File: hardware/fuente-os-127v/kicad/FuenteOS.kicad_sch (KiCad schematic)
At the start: 10 parts, among them J1 127 VCA, J2 SALIDA OS

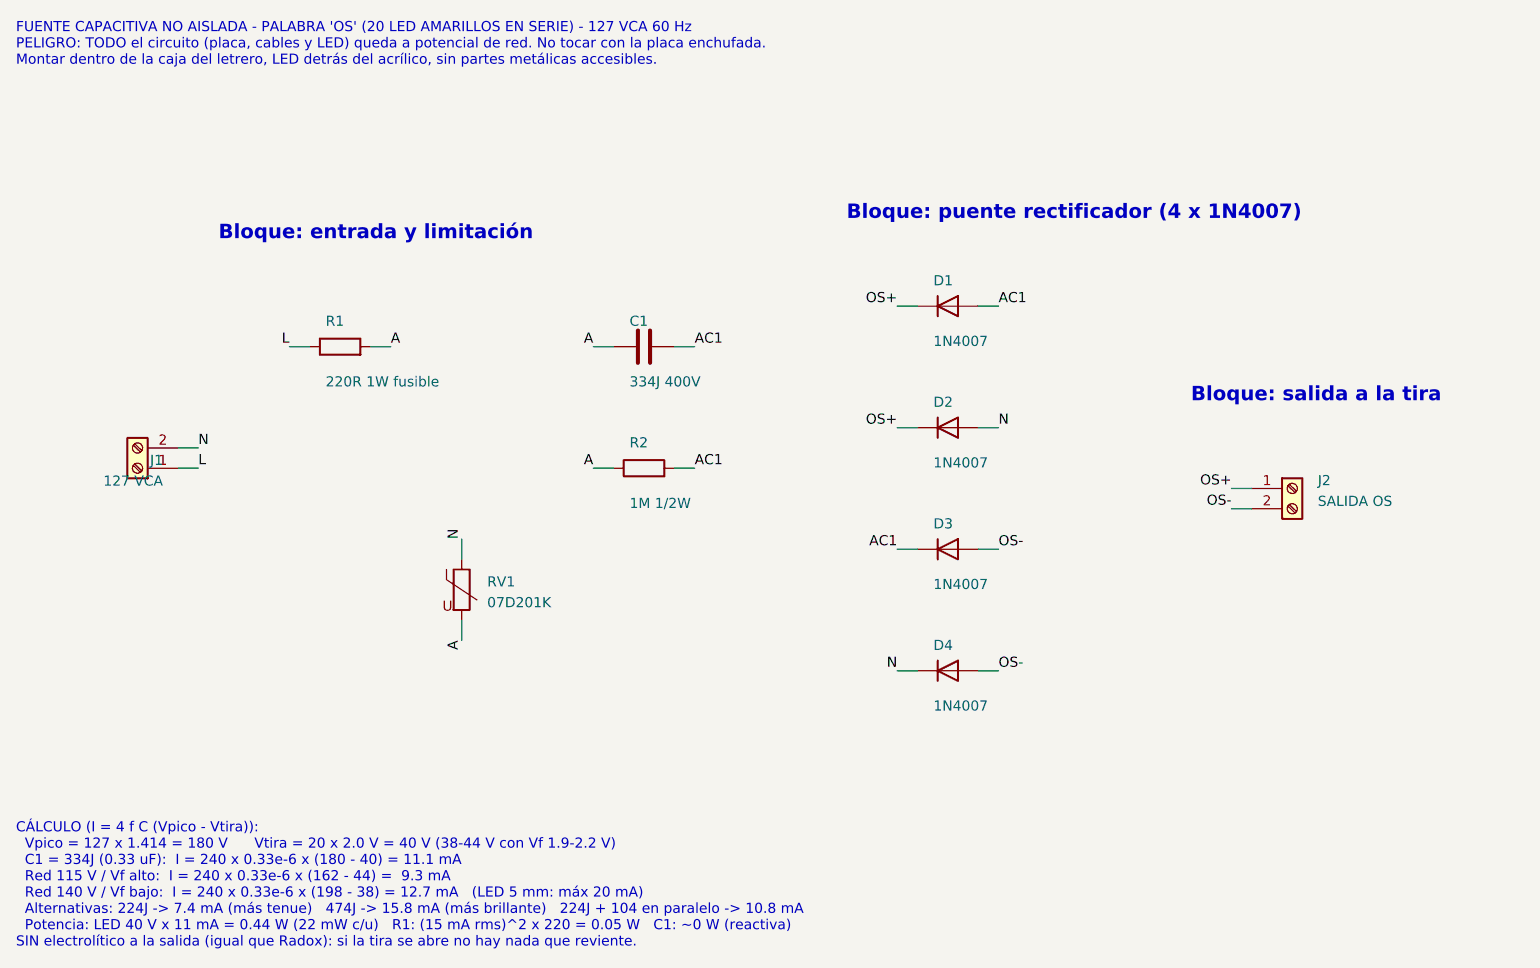
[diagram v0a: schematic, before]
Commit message: Placa OS v2 (27 LED, puente 2W10, capacitor paso 10/15 mm) y secuenciador de flechas 127 VCA
- fuente-os-127v: O (13) + S (14) = 27 LED; C1 334J -> 10 mA (474J si son blanco
  calido); puente redondo 2W10; huella de capacitor con barrenos a 10 y 15 mm.
- flechas-127v: NE555 + CD4017 + 3 SCR MCR100-6, dos fuentes capacitivas con
  2W10 (logica 474J + zener 12 V, flechas 224J ~8 mA). PCB 50x60 mm una cara,
  2 puentes de alambre; ERC/DRC 0 con paridad; PDF 1:1 para planchar, Gerber,
  Excellon, BOM.
- gen/comun.py: huellas, esquema, PCB, ruteo y separacion de redes por puentes
  compartidos por ambas placas.

Co-Authored-By: Claude Opus 5.5 <noreply@anthropic.com>
Claude-Session: https://claude.ai/code/session_01WVk3oGwfQfGTmAT2PMp8oW
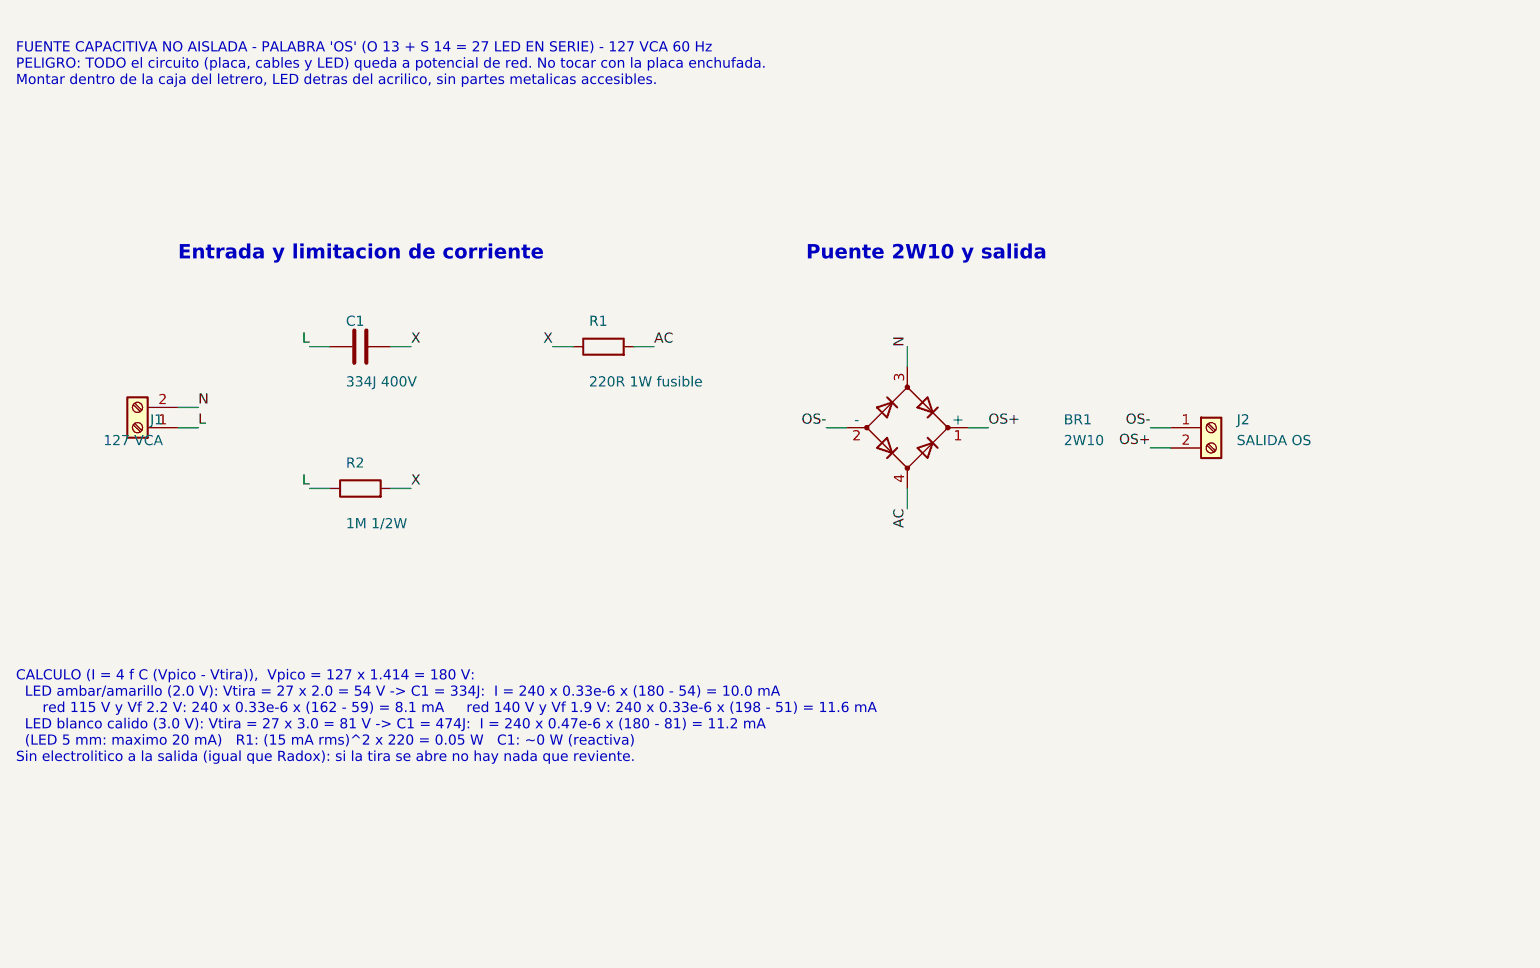
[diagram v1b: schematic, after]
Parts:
- removed D1, D2, D3, D4: 1N4007, FuenteOS:D_DO-41_P10.16mm, symbol Device:D
- removed RV1: 07D201K, FuenteOS:Varistor_D7mm_P5mm, symbol Device:Varistor
- added BR1: 2W10, FuenteOS:Puente_2W10, symbol Device:D_Bridge_+-AA
- C1: footprint FuenteOS:C_Poliester_P15mm -> FuenteOS:C_Poliester_P10-15mm; Funcion Capacitor de poliéster 0.33 uF 400 V: fija la corriente de 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 -> Poliester 0.33 uF 400 V (paso 10 o 15 mm): fija la corrient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
- J1: Funcion Entrada de red 127 VCA (pin 1 = L fase, pin 2 = N neutro). Tomar del mismo cable que la placa Radox -> Entrada de red 127 VCA (pin 1 = L fase, pin 2 = N neutro). Del mismo cable que la placa Radox
- J2: Funcion Salida a la palabra OS: 20 LED amarillos en serie (pin 1 = 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 -> Salida a O+S (27 LED en serie): pin 2 = + (anodo del primer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
- R1: footprint FuenteOS:R_1W_P15.24mm -> FuenteOS:R_1W_Vertical_P7.62mm; Funcion Resistencia fusible (flameproof): limita el pico al enchufar (180 V / 220 = 0.8 A) y actúa como fusible -> Resistencia fusible (flameproof): limita el pico al enchufar (180 V / 220 = 0.8 A) y actua como fusible
- R2: footprint FuenteOS:R_Axial_P15.24mm -> FuenteOS:R_Axial_P10.16mm
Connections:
- net L: now also C1.1, R2.1; no longer R1.1
- net N: now also BR1.3
- net OS+: now also J2.2 (Pin_2), BR1.1 (+); no longer J2.1 (Pin_1)
- net OS-: now also J2.1 (Pin_1), BR1.2 (-); no longer J2.2 (Pin_2)
- removed net A: C1.1, R1.2, R2.1
- net AC1 renamed X
- net X: now also R1.1
- new net AC: BR1.4, R1.2
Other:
- note added: "CALCULO (I = 4 f C (Vpico - Vtira)), Vpico = 127 x 1.414 = 180 V: LED ambar/amarillo (2.0 V): Vtira = 27 x 2.0 = 54 V -> C1 = 334J: I = 240 x 0.33e-6 x (180 - 54) = 10.0 mA red 115 V y Vf 2.2 V: 240 x 0.33e-6 x (162 - 59) = 8.1 mA red 140 V y Vf 1.9 V: 240 x 0.33e-6 x (198 - 51) = 11.6 mA LED blanco calido (3.0 V): Vtira = 27 x 3.0 = 81 V -> C1 = 474J: I = 240 x 0.47e-6 x (180 - 81) = 11.2 mA (LE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"
- note added: "Entrada y limitacion de corriente"
- note added: "FUENTE CAPACITIVA NO AISLADA - PALABRA 'OS' (O 13 + S 14 = 27 LED EN SERIE) - 127 VCA 60 Hz PELIGRO: TODO el circuito (placa, cables y LED) queda a potencial de red. No tocar con la placa enchufada. Montar dentro de la caja del letrero, LED detras del acrilico, sin partes metalicas accesibles."
- note added: "Puente 2W10 y salida"
- note removed: "Bloque: entrada y limitación"
- note removed: "Bloque: puente rectificador (4 x 1N4007)"
- note removed: "Bloque: salida a la tira"
- note removed: "CÁLCULO (I = 4 f C (Vpico - Vtira)): Vpico = 127 x 1.414 = 180 V Vtira = 20 x 2.0 V = 40 V (38-44 V con Vf 1.9-2.2 V) C1 = 334J (0.33 uF): I = 240 x 0.33e-6 x (180 - 40) = 11.1 mA Red 115 V / Vf alto: I = 240 x 0.33e-6 x (162 - 44) = 9.3 mA Red 140 V / Vf bajo: I = 240 x 0.33e-6 x (198 - 38) = 12.7 mA (LED 5 mm: máx 20 mA) Alternativas: 224J -> 7.4 mA (más tenue) 474J -> 15.8 mA (más brillante) 2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"
- note removed: "FUENTE CAPACITIVA NO AISLADA - PALABRA 'OS' (20 LED AMARILLOS EN SERIE) - 127 VCA 60 Hz PELIGRO: TODO el circuito (placa, cables y LED) queda a potencial de red. No tocar con la placa enchufada. Montar dentro de la caja del letrero, LED detrás del acrílico, sin partes metálicas accesibles."
- title: Fuente capacitiva 127 VCA para la palabra OS (20 LED amarillos) -> Fuente capacitiva 127 VCA para la palabra OS (27 LED)
- moved on the sheet: C1, J1, J2, R1, R2
